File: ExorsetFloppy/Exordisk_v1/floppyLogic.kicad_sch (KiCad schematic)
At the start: 76 parts, among them J10 Conn_01x01, J11 Conn_01x01, J12 Conn_01x01, J13 Conn_01x01, J14 Conn_01x01, J15 Conn_01x01, J16 Conn_01x01, J17 Conn_01x01, J18 Conn_01x01, J19 Conn_01x01, J2 Floppy, J20 Conn_01x01, J21 Conn_01x01, J22 Conn_01x01, J3 Conn_01x01, J7 Conn_01x17, J8 Conn_01x01, J9 Conn_01x01, Q1 BC337, U10 GAL16V8, U11 74HCT74, U12 74HCT74, U13 74LS91, U15 74HCT04, U16 74HCT74, U17 74HCT00, U18 74HCT74, U19 74LS76, U2 74HCT74, U20 68B21, U21 MC4024, U22 74LS157, U23 74LS123, U24 74HCT164, U25 74LS04, U27 MC4044, U28 74F163, U29 74F163, U34 6852_DIL24, U4 MC8506, U5 74F163, U7 74HCT240, U8 74HCT244, U9 NE7555P

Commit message: new schematic for exordisk
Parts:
- removed C20: 10n, Capacitor_SMD:C_1206_3216Metric_Pad1.33x1.80mm_HandSolder, symbol Device:C_Small
- removed C21: 1u, Capacitor_SMD:C_1206_3216Metric_Pad1.33x1.80mm_HandSolder, symbol Device:C_Polarized_Small
- removed D3: BAS40-04, Package_TO_SOT_SMD:SOT-23_Handsoldering, symbol Diode:BAS40-04
- removed J19: Conn_01x01, Connector_PinHeader_2.54mm:PinHeader_1x01_P2.54mm_Vertical, symbol Connector_Generic:Conn_01x01
- removed JP6: Jumper_3_Open, Jumper:SolderJumper-3_P1.3mm_Open_RoundedPad1.0x1.5mm_NumberLabels, symbol Jumper:Jumper_3_Open
- removed R2: 10M, Resistor_SMD:R_1206_3216Metric_Pad1.30x1.75mm_HandSolder, symbol Device:R_Small
- removed U13: 74LS91, Package_DIP:DIP-14_W7.62mm, symbol 74xx:74LS91
- removed U19: 74LS76, Package_DIP:DIP-16_W7.62mm, symbol 74xx:74LS76
- removed unit 3 of U21
- removed U4: MC8506, Package_DIP:DIP-16_W7.62mm, symbol my_ics_new:MC8506
- removed U9: NE7555P, Package_DIP:DIP-8_W7.62mm, symbol Timer:NE555P
- added J19: Conn_02x02_Odd_Even, Connector_PinHeader_2.54mm:PinHeader_2x02_P2.54mm_Vertical, symbol Connector_Generic:Conn_02x02_Odd_Even
- added J23, J24, J25, J26, J27, J28, J29, J30, J31, J32, J33, J34, J35, J36, J37, J38, J39, J40, J41: Conn_01x01, Connector_PinHeader_2.54mm:PinHeader_1x01_P2.54mm_Vertical, symbol Connector_Generic:Conn_01x01
- added U19: 74LS73, Package_DIP:DIP-14_W7.62mm, symbol 74xx:74LS73
- added U4: MC8506_new, Package_DIP:DIP-16_W7.62mm, symbol my_ics_new:MC8506_new
- J10, J11, J12, J13, J14, J15, J16, J17, J18, J21, J22, J3, J8, J9: footprint Connector_PinHeader_1.27mm:PinHeader_1x01_P1.27mm_Vertical -> Connector_PinHeader_2.54mm:PinHeader_1x01_P2.54mm_Vertical
- R3: value 27k -> 47k
- R4: value 47k -> 100k
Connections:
- net +5V: now also U23.10 (B), U23.2 (B), U4.16 (Vcc); no longer J3.1 (Pin_1)
- net 8x_RD_CLK: now also J24.1 (Pin_1), U19.1 (C)
- net A0#: now also U20.35 (RS1); no longer U20.36 (RS0)
- net A1#: now also U20.36 (RS0); no longer U20.35 (RS1)
- net CRC-0: now also J35.1 (Pin_1)
- net CRC_DOUT: now also U4.11 (D_Out)
- net CRC_RDAT: now also J34.1 (Pin_1), U4.12 (RD)
- net D0: now also U34.15 (D7); no longer U34.22 (D0)
- net D1: now also U34.16 (D6); no longer U34.21 (D1)
- net D2: now also U34.17 (D5); no longer U34.20 (D2)
- net D3: now also U34.18 (D4); no longer U34.19 (D3)
- net D4: now also U34.19 (D3); no longer U34.18 (D4)
- net D5: now also U34.20 (D2); no longer U34.17 (D5)
- net D6: now also U34.21 (D1); no longer U34.16 (D6)
- net D7: now also U34.22 (D0); no longer U34.15 (D7)
- net F: now also J23.1 (Pin_1)
- net GND: now also J19.1 (Pin_1), J19.2 (Pin_2), J19.3 (Pin_3), J19.4 (Pin_4), U19.3 (K), U4.10 (INV), U4.8 (GND); no longer J20.1 (Pin_1), U23.10 (B), U23.2 (B)
- net HLD: now also J36.1 (Pin_1)
- net RESET: now also U19.2 (~{R})
- net SM_Latch: now also J27.1 (Pin_1), U19.12 (Q)
- net TUF: now also J38.1 (Pin_1)
- net TXD: now also J37.1 (Pin_1), U4.14 (WD)
- net WPROT: now also U8.5 (O2b); no longer U7.16 (O1a)
- net WRITE/~{READ}: now also U4.13 (R/W)
- net ~{EN_CRC}: now also U4.6 (~{E})
- net ~{RESET}: now also J40.1 (Pin_1), U4.15 (P)
- net ~{SM_Latch}: now also J30.1 (Pin_1), U19.13 (~{Q})
- net ~{WPT}: now also U8.15 (I2b); no longer U7.4 (I1a)
- net at U10.2 (I2), U2.6 (~{Q}): now also J29.1 (Pin_1)
- net at U34.5 (SM/~{DTR}): now also J26.1 (Pin_1), U19.14 (J)
- net Q3: now reaches U5.11 (Q3)
- net Q3: now also U11.11 (C), U15.1, U2.11 (C), U2.3 (C), J28.1 (Pin_1)
- net at U22.4 (Za), U5.9 (~{PE}): now also J41.1 (Pin_1)
- net at U11.8 (~{Q}), U17.12, U22.10 (I1c): now also J39.1 (Pin_1)
- net at C39.1, U27.3 (V), U28.15 (TC): now also J25.1 (Pin_1)
- net at U25.2, U34.3 (RXClk), U34.4 (TXClk): now also J20.1 (Pin_1)
- net at J8.1 (Pin_1): now also U7.4 (I1a); no longer U8.15 (I2b)
- net at J9.1 (Pin_1): now also U7.16 (O1a); no longer U8.5 (O2b)
- net at U16.9 (Q): now also U4.9 (Shift)
- net at U17.6: now also J31.1 (Pin_1), U4.5 (~{RCLK})
- net at U11.2 (D): now also J33.1 (Pin_1), U4.2 (~{AZ})
- net at U11.3 (C), U15.2: now also J32.1 (Pin_1)
- net at R1.2: now also U4.7 (PS)
- removed net CLK_U5_15: U11.11 (C), U15.1, U2.11 (C), U2.3 (C), U5.15 (TC)
- net SLOW renamed Q0
- net Q0: now also J3.1 (Pin_1), U4.4 (~{WCLK})
- no-connect marks 41 -> 39
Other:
- note added: "1A"
- note added: "1B"
- note added: "1C"
- note added: "1D"
- note added: "1E,2A,3A"
- note added: "1F"
- note added: "1G"
- note added: "1H"
- note added: "1J,2B,3B"
- note added: "2C,4I"
- note added: "2D,3C"
- note added: "2E"
- note added: "2F,4D"
- note added: "2G,4E"
- note added: "2H"
- note added: "3D"
- note added: "3E"
- note added: "3F"
- note added: "3G"
- note added: "3H"
- note added: "3I"
- note added: "4B"
- note added: "4C"
- note added: "4F"
- note added: "4G"
- note added: "4N"
- note added: "CRC Latch"
- note added: "Maybe use a second '244 and a '04 for the input signals and as inverter for the MOT signal. Also: connect the HLD Signal."
- note added: "Problems (needs fixing in next Version): U23-2 and U23-10 needs to go to +5V - done R4 from 47k -> 220k, R3 27k -> 47k - done U5-15 wrong, needs to go to U5-11 - done maybe more Testpoints - look in AN764, SEL2, SEL3 and WPT should NOT be inverted - WPT done U34 has Datalines switched: D0->D7, D1->D6,... - done U20 A0 and A1 are switched - done U14 forgot +5V on Pin 14 and GND on Pin 7 - deleted 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"
- note added: "V"
- note removed: "A"
- note removed: "B"
- note removed: "C"
- note removed: "D"
- note removed: "G"
- note removed: "H"
- note removed: "I used a 74HCT73 instead of the '76. Different Pinout though!"
- note removed: "J"
- note removed: "JK-FF"
- note removed: "PROBLEM Double Pin15 - RdCLK is Pin 5, Double Pin8,"
- note removed: "Problems (needs fixing in next Version): U23-2 and U23-10 needs to go to +5V, R4 from 47k -> 100k, C7 from 100u -> 220u, U5-15 wrong, needs to go to U5-11, maybe more Testpoints - look in AN764, SEL2, SEL3 and WPT should NOT be inverted, U34 has Datalines switched: D0->D7, D1->D6,..., U20 A0 and A1 are switched, U14 forgot +5V on Pin 14 and GND on Pin 7, U21-13 must conn. to GND (or maybe open?),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"
- note removed: "Testpoint missing! (C)"
- note removed: "Testpoints missing! (En_CRC and not Q)"
- note removed: "Testpoints missing! (Q0 and Q3)"
- note removed: "Testpoints missing! (Sync Match and SM Latch Q and not Q)"
- note removed: "Use U23A instead of U9! Tested the '123 and it works fine. Ditch the NE555!"
- note removed: "Use a second '244 and a '04 for the input signals and as inverter for the MOT signal. Also: connect the HLD Signal."
- note removed: "WPROT is wrong. It is Write Enabled in orig. schem."
- moved on the sheet: J21, J3, J8, J9, R1, U11A, U12B, U15A, U16B, U17B, U17C, U24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

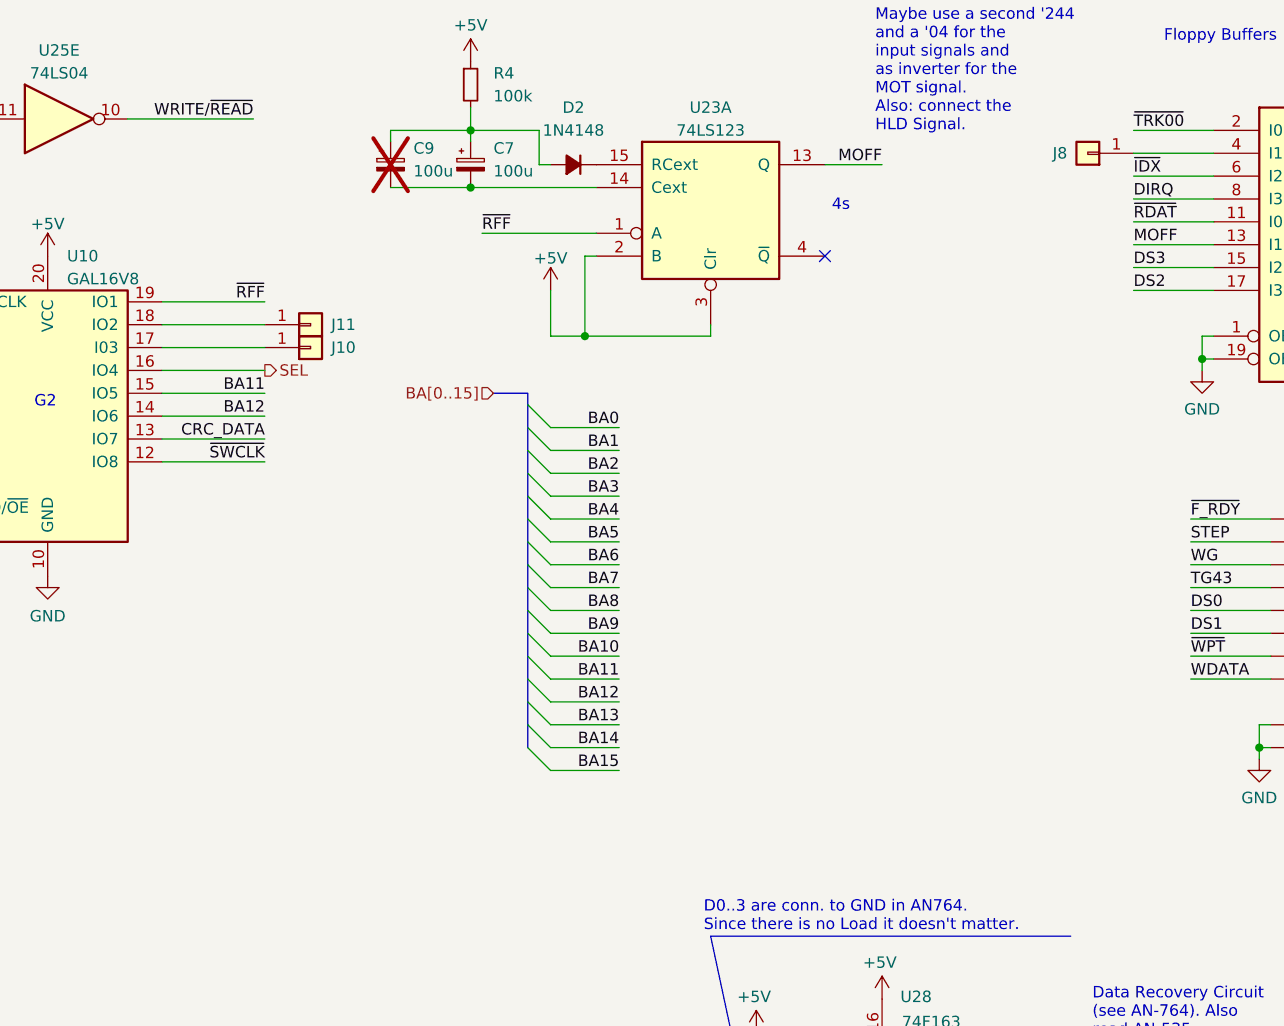
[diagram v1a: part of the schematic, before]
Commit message: new GAL eq. for additional EPROM on board
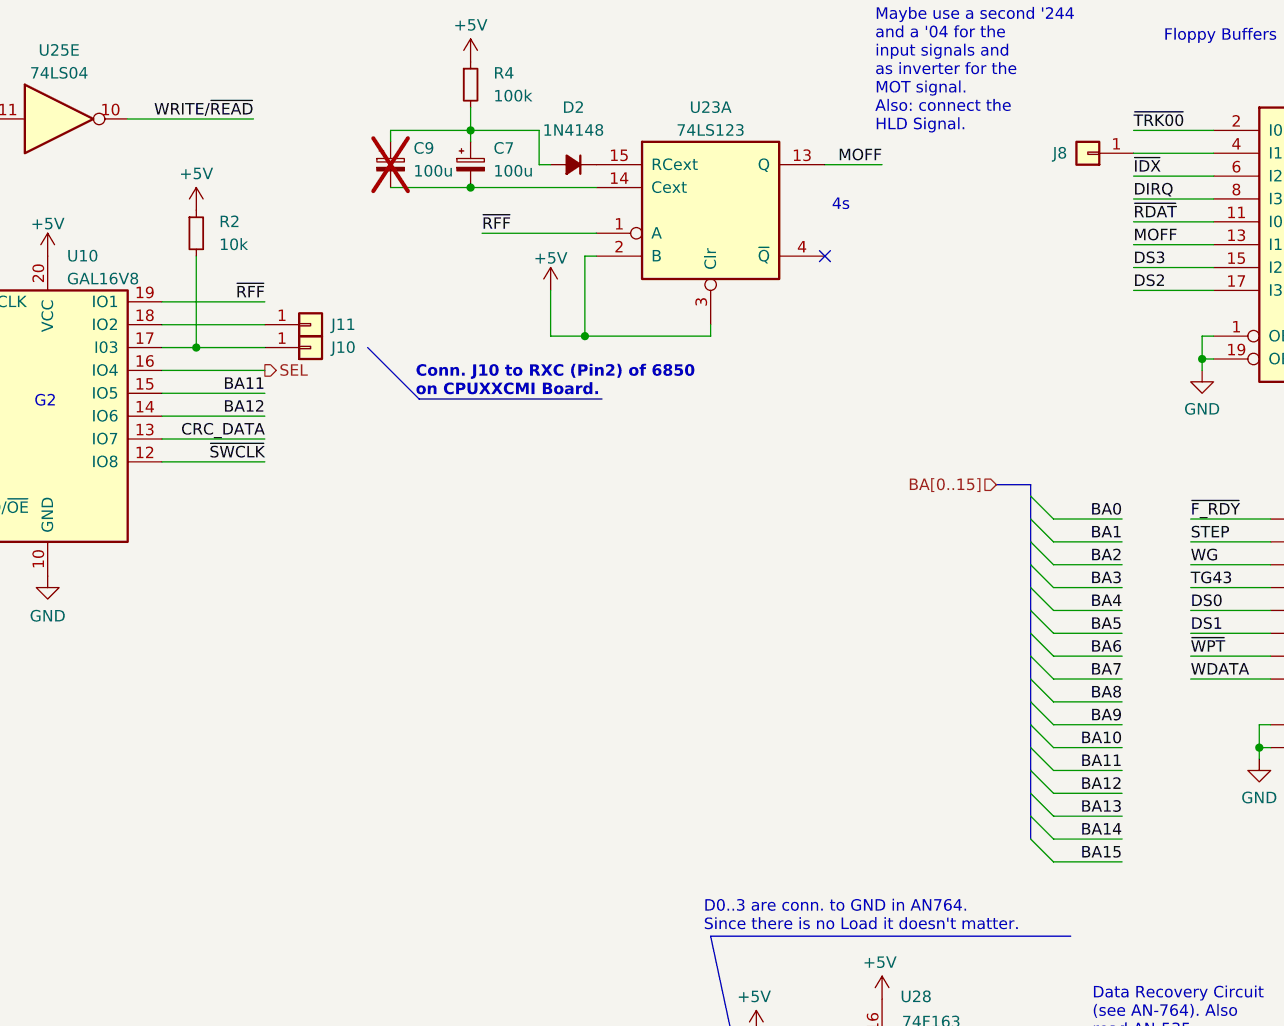
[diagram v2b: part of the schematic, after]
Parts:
- added R2: 10k, Resistor_SMD:R_1206_3216Metric_Pad1.30x1.75mm_HandSolder, symbol Device:R_Small
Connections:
- net +5V: now also R2.1
- net at J10.1 (Pin_1), U10.17 (I03): now also R2.2
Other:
- note added: "Conn. J10 to RXC (Pin2) of 6850 on CPUXXCMI Board."

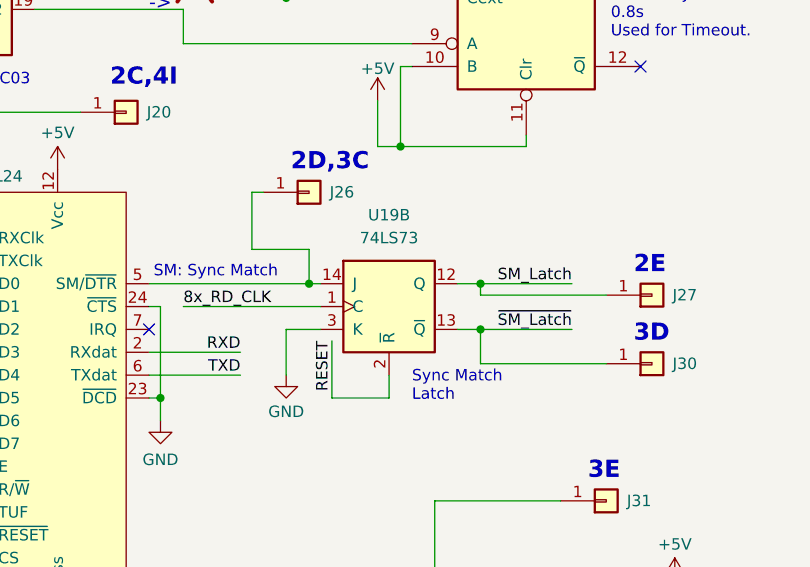
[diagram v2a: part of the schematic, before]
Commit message: 74LS73 ch. to LS112
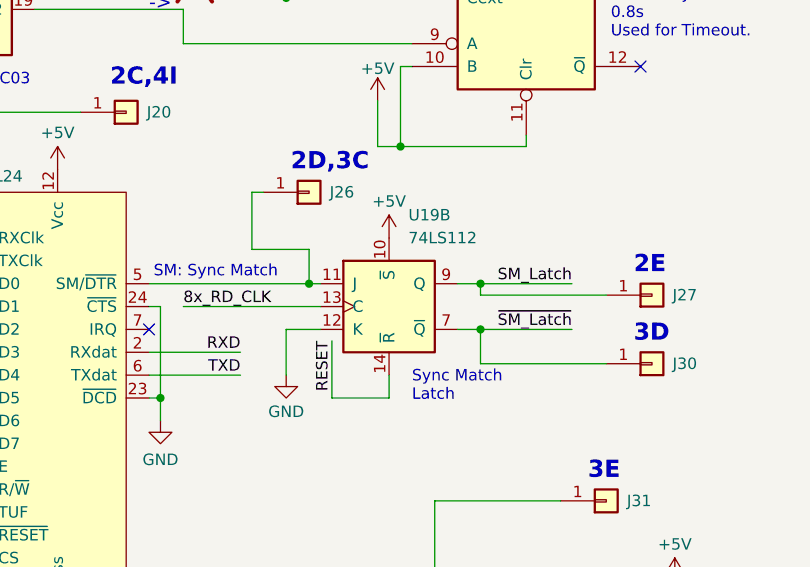
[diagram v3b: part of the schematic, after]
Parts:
- removed U19: 74LS73, Package_DIP:DIP-14_W7.62mm, symbol 74xx:74LS73
- added U19: 74LS112, Package_DIP:DIP-16_W7.62mm, symbol 74xx:74LS112
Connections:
- net +5V: now also U19.10 (~{S})
- net 8x_RD_CLK: now also U19.13 (C)
- net GND: now also U19.12 (K)
- net RESET: now also U19.14 (~{R})
- net SM_Latch: now also U19.9 (Q)
- net ~{SM_Latch}: now also U19.7 (~{Q})
- net at J26.1 (Pin_1), U34.5 (SM/~{DTR}): now also U19.11 (J)
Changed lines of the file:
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@@
 	)
 	(symbol
+		(lib_id "power:+5V")
+		(at 93.98 106.68 0)
+		(unit 1)
+		(exclude_from_sim no)
+		(in_bom yes)
+		(on_board yes)
+		(dnp no)
+		(property "Reference" "#PWR066"
+			(at 93.98 110.49 0)
+			(effects
+				(font
+					(size 1.27 1.27)
+				)
+				(hide yes)
+			)
+		)
+		(property "Value" "+5V"
+			(at 93.98 102.616 0)
+			(effects
+				(font
+					(size 1.27 1.27)
+				)
+			)
+		)
+		(property "Footprint" ""
+			(at 93.98 106.68 0)
+			(effects
+				(font
+					(size 1.27 1.27)
+				)
+				(hide yes)
+			)
+		)
+		(property "Datasheet" ""
+			(at 93.98 106.68 0)
+			(effects
+				(font
+					(size 1.27 1.27)
+				)
+				(hide yes)
+			)
+		)
+		(property "Description" "Power symbol creates a global label with name \"+5V\""
+			(at 93.98 106.68 0)
+			(effects
+				(font
+					(size 1.27 1.27)
+				)
+				(hide yes)
+			)
+		)
+		(pin "1"
+		)
+		(instances
+			(project "Exordisk_v1"
+				(path "/05fb24d5-db99-47c3-b50e-9b588fa507ac/a1c0351e-a831-4754-8be5-6f4bd5bad354"
+					(reference "#PWR066")
+					(unit 1)
+				)
+			)
+		)
+	)
+	(symbol
 		(lib_id "Connector_Generic:Conn_01x01")
 		(at 306.07 179.07 0)
@@
 	)
 	(symbol
+		(lib_id "74xx:74LS112")
+		(at 93.98 114.3 0)
+		(unit 2)
+		(exclude_from_sim no)
+		(in_bom yes)
+		(on_board yes)
+		(dnp no)
+		(fields_autoplaced yes)
+		(property "Reference" "U19"
+			(at 96.1233 104.14 0)
+			(effects
+				(font
+					(size 1.27 1.27)
+				)
+				(justify left)
+			)
+		)
+		(property "Value" "74LS112"
+			(at 96.1233 106.68 0)
+			(effects
+				(font
+					(size 1.27 1.27)
+				)
+				(justify left)
+			)
+		)
+		(property "Footprint" "Package_DIP:DIP-16_W7.62mm"
+			(at 93.98 114.3 0)
+			(effects
+				(font
+					(size 1.27 1.27)
+				)
+				(hide yes)
+			)
+		)
+		(property "Datasheet" "http://www.ti.com/lit/gpn/sn74LS112"
+			(at 93.98 114.3 0)
+			(effects
+				(font
+					(size 1.27 1.27)
+				)
+				(hide yes)
+			)
+		)
+		(property "Description" "dual JK Flip-Flop, Set & Reset"
+			(at 93.98 114.3 0)
+			(effects
+				(font
+					(size 1.27 1.27)
+				)
+				(hide yes)
+			)
+		)
+		(pin "13"
+		)
+		(pin "8"
+		)
+		(pin "11"
+		)
+		(pin "14"
+		)
+		(pin "9"
+		)
+		(pin "7"
+		)
+		(pin "6"
+		)
+		(pin "5"
+		)
+		(pin "15"
+		)
+		(pin "4"
+		)
+		(pin "2"
+		)
+		(pin "1"
+		)
+		(pin "10"
+		)
+		(pin "12"
+		)
+		(pin "3"
+		)
+		(pin "16"
+		)
+		(instances
+			(project "Exordisk_v1"
+				(path "/05fb24d5-db99-47c3-b50e-9b588fa507ac/a1c0351e-a831-4754-8be5-6f4bd5bad354"
+					(reference "U19")
+					(unit 2)
+				)
+			)
+		)
+	)
+	(symbol
 		(lib_id "Device:C_Polarized_Small")
 		(at 82.55 77.47 0)
@@
 				)
 			)
-		)
-	)
-	(symbol
-		(lib_id "74xx:74LS73")
-		(at 93.98 114.3 0)
-		(unit 2)
-		(exclude_from_sim no)
-		(in_bom yes)
-		(on_board yes)
-		(dnp no)
-		(fields_autoplaced yes)
-		(property "Reference" "U19"
-			(at 93.98 104.14 0)
-			(effects
-				(font
-					(size 1.27 1.27)
-				)
-			)
-		)
-		(property "Value" "74LS73"
-			(at 93.98 106.68 0)
-			(effects
-				(font
-					(size 1.27 1.27)
-				)
-			)
-		)
-		(property "Footprint" "Package_DIP:DIP-14_W7.62mm"
-			(at 93.98 114.3 0)
-			(effects
-				(font
-					(size 1.27 1.27)
-				)
-				(hide yes)
-			)
-		)
-		(property "Datasheet" "http://www.ti.com/lit/gpn/sn74LS73"
-			(at 93.98 114.3 0)
-			(effects
-				(font
-					(size 1.27 1.27)
-				)
-				(hide yes)
-			)
-		)
-		(property "Description" "Dual JK Flip-Flop, reset"
-			(at 93.98 114.3 0)
-			(effects
-				(font
-					(size 1.27 1.27)
-				)
-				(hide yes)
-			)
-		)
-		(pin "2"
-		)
-		(pin "5"
-		)
-		(pin "7"
-		)
-		(pin "1"
-		)
-		(pin "3"
-		)
-		(pin "11"
-		)
-		(pin "12"
-		)
-		(pin "4"
-		)
-		(pin "13"
-		)
-		(pin "10"
-		)
-		(pin "9"
-		)
-		(pin "6"
-		)
-		(pin "14"
-		)
-		(pin "8"
-		)
-		(instances
-			(project "Exordisk_v1"
-				(path "/05fb24d5-db99-47c3-b50e-9b588fa507ac/a1c0351e-a831-4754-8be5-6f4bd5bad354"
-					(reference "U19")
-					(unit 2)
-				)
-			)

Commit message: build script new
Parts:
- added J42, J43: Conn_01x01, Connector_PinHeader_2.54mm:PinHeader_1x01_P2.54mm_Vertical, symbol Connector_Generic:Conn_01x01
- added U9: 74LS138, Package_DIP:DIP-16_W7.62mm, symbol 74xx:74LS138
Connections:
- net +5V: now also U9.16 (VCC), U9.6 (E3)
- net DS0: now also U9.1 (A0); no longer U8.11 (I0b)
- net DS1: now also U9.2 (A1); no longer U8.13 (I1b)
- net DS2: now also J42.1 (Pin_1); no longer U7.17 (I3b)
- net DS3: now also J43.1 (Pin_1); no longer U7.15 (I2b)
- net GND: now also U9.3 (A2), U9.4 (E1), U9.8 (GND)
- net HLD: now also U9.5 (E2)
- net ~{DS0}: now also U9.13 (O2); no longer U8.9 (O0b)
- net ~{DS1}: now also U9.14 (O1); no longer U8.7 (O1b)
- net ~{DS2}: now also U9.15 (O0); no longer U7.3 (O3b)
- net ~{DS3}: now also U9.12 (O3); no longer U7.5 (O2b)
- no-connect marks 39 -> 43
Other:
- note added: "DS0,1 should be inverted in the code."
- note added: "x x"
